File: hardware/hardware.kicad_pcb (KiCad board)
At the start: 4 copper layers, 60 x 71 mm, 100 parts, among them J1 Conn_Coaxial, J10 Conn_Coaxial, J11 Conn_01x06_Pin, J2 BOOT, J3 SWD, J4 Conn_Coaxial, J5 Conn_Coaxial, J6 Conn_Coaxial, J7 Conn_Coaxial, J8 Conn_Coaxial, J9 Conn_Coaxial, SW1 SW_Push, U11 24LC32, U13 24LC32, U15 24LC32, U17 24LC32, U2 STM32F103C8Tx, U3 24LC32, U5 24LC32, U7 24LC32, U9 24LC32, Y2 Crystal_GND24

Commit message: add GM capacitor + vbat to 3.3 + move osc on correct pins on stm32
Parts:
- added C1: C_Small, Capacitor_SMD:C_0603_1608Metric, F.Cu at (133.4, 85.0)
- added C11: C_Small, Capacitor_SMD:C_0603_1608Metric, F.Cu at (116.4, 88.4)
- added C12: C_Small, Capacitor_SMD:C_1206_3216Metric, F.Cu at (105.4, 84.2)
- added C13: C_Small, Capacitor_SMD:C_0603_1608Metric, F.Cu at (105.0, 88.2)
- added C14: C_Small, Capacitor_SMD:C_1206_3216Metric, F.Cu at (92.4, 84.4)
- added C15: C_Small, Capacitor_SMD:C_0603_1608Metric, F.Cu at (92.6, 88.2)
- added C16: C_Small, Capacitor_SMD:C_1206_3216Metric, F.Cu at (150.9, 113.4)
- added C17: C_Small, Capacitor_SMD:C_0603_1608Metric, F.Cu at (155.8, 109.6)
- added C18: C_Small, Capacitor_SMD:C_1206_3216Metric, F.Cu at (150.9, 116.7)
- added C19: C_Small, Capacitor_SMD:C_0603_1608Metric, F.Cu at (155.8, 112.1)
- added C2: C_Small, Capacitor_SMD:C_1206_3216Metric, F.Cu at (131.4, 84.4)
- added C20: C_Small, Capacitor_SMD:C_1206_3216Metric, F.Cu at (150.9, 120.1)
- added C21: C_Small, Capacitor_SMD:C_0603_1608Metric, F.Cu at (155.8, 114.6)
- added C22: C_Small, Capacitor_SMD:C_1206_3216Metric, F.Cu at (150.9, 123.4)
- added C23: C_Small, Capacitor_SMD:C_0603_1608Metric, F.Cu at (155.8, 117.1)
- added C3: C_Small, Capacitor_SMD:C_1206_3216Metric, F.Cu at (118.4, 84.2)
- moved C9 6.51 mm to (100.6, 107.6)
- moved C10 5.37 mm to (96.2, 103.2)
- moved Y2 0.57 mm to (98.4, 105.4), turned to -45 degrees
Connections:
- U1 pad 6: unconnected-(U1-VBAT-Pad6) -> +3.3V
- U10 pad 6: unconnected-(U10-VBAT-Pad6) -> +3.3V
- U12 pad 6: unconnected-(U12-VBAT-Pad6) -> +3.3V
- U14 pad 6: unconnected-(U14-VBAT-Pad6) -> +3.3V
- U16 pad 6: unconnected-(U16-VBAT-Pad6) -> +3.3V
- U2 pad 2: OSIN -> unconnected-(U2-PC13-Pad2)
- U2 pad 3: OSOUT -> unconnected-(U2-PC14-Pad3)
- U2 pad 5: unconnected-(U2-PD0-Pad5) -> OSOUT
- U2 pad 6: unconnected-(U2-PD1-Pad6) -> OSIN
- U4 pad 6: unconnected-(U4-VBAT-Pad6) -> +3.3V
- U6 pad 6: unconnected-(U6-VBAT-Pad6) -> +3.3V
- U8 pad 6: unconnected-(U8-VBAT-Pad6) -> +3.3V
- Y2 pad 1: GND -> OSOUT
- Y2 pad 2: OSIN -> GND
- Y2 pad 3: GND -> OSIN
- Y2 pad 4: OSOUT -> GND
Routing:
- net +3.3V: track 106.1 -> 153.2 mm, vias 39 -> 35
- net GND: track 256.8 -> 263.2 mm
- net OSOUT: track 6.82 -> 7.36 mm

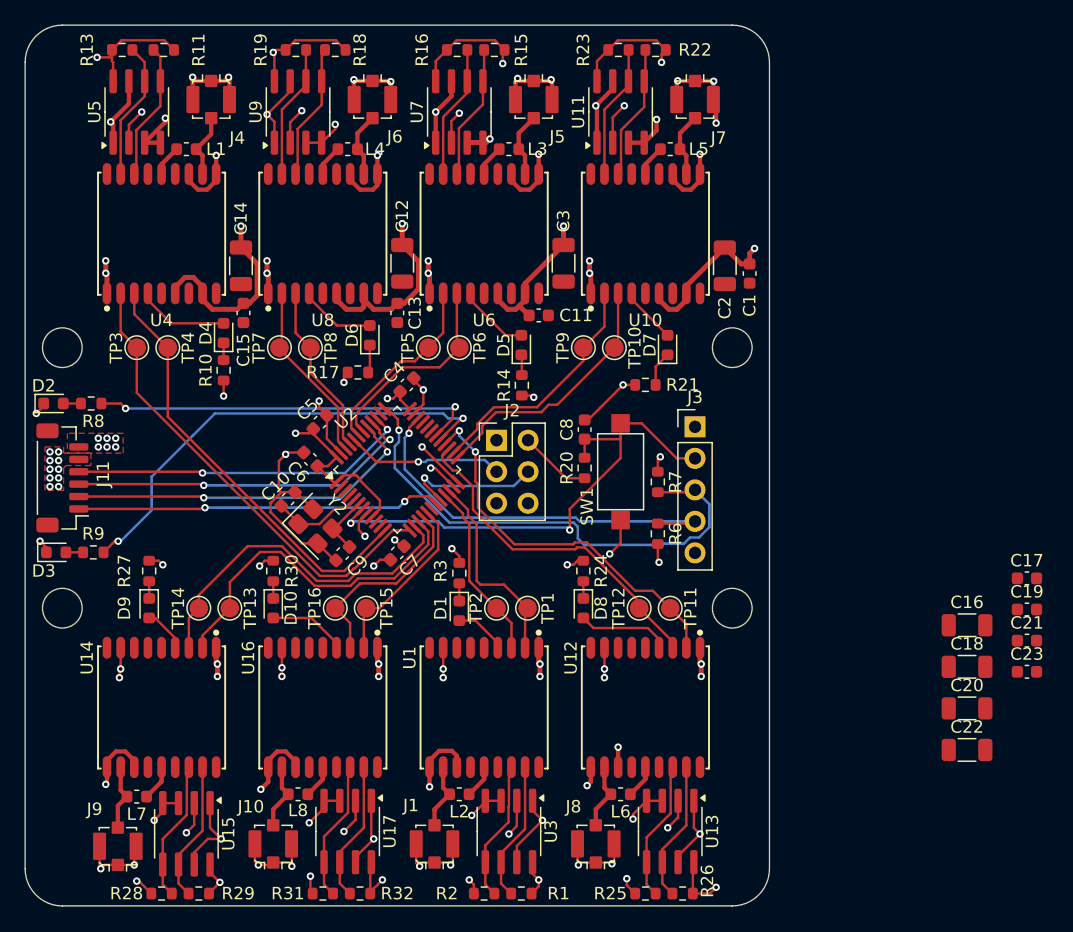
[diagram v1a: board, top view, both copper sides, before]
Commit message: fix swdio programming
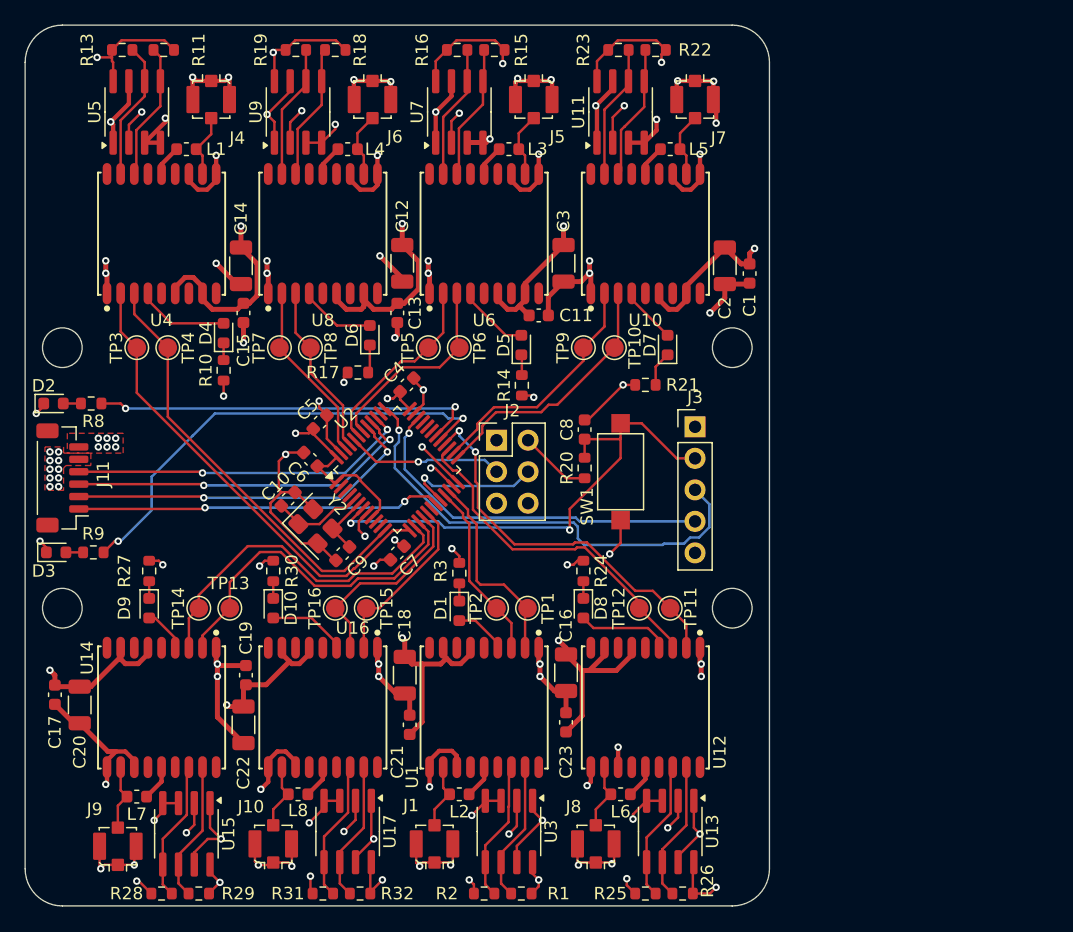
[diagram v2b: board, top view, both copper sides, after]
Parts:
- removed R6, R7: 10k, Resistor_SMD:R_0603_1608Metric
- moved C17 78.9 mm to (77.4, 119.0), turned to -90 degrees
- moved C20 71.5 mm to (79.4, 119.8), turned to 90 degrees
- moved C19 63.2 mm to (92.8, 117.4), turned to 90 degrees
- moved C22 58.4 mm to (92.6, 121.4), turned to 90 degrees
- moved C21 50.2 mm to (106.0, 121.4), turned to 90 degrees
- moved C18 45.3 mm to (105.6, 117.4), turned to 90 degrees
- moved C23 37.4 mm to (118.6, 121.2), turned to 90 degrees
- moved C16 32.6 mm to (118.6, 117.2), turned to 90 degrees
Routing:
- net +3.3V: track 153.2 -> 197.7 mm, vias 35 -> 30
- net GND: track 263.2 -> 304.6 mm, vias 94 -> 98
- net SWDIO: track 32.8 -> 30.0 mm
- net SWCLK: track 41.1 -> 38.3 mm
